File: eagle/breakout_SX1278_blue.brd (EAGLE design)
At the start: 28.6 x 28.6 mm, 18 parts, among them X1 734120110

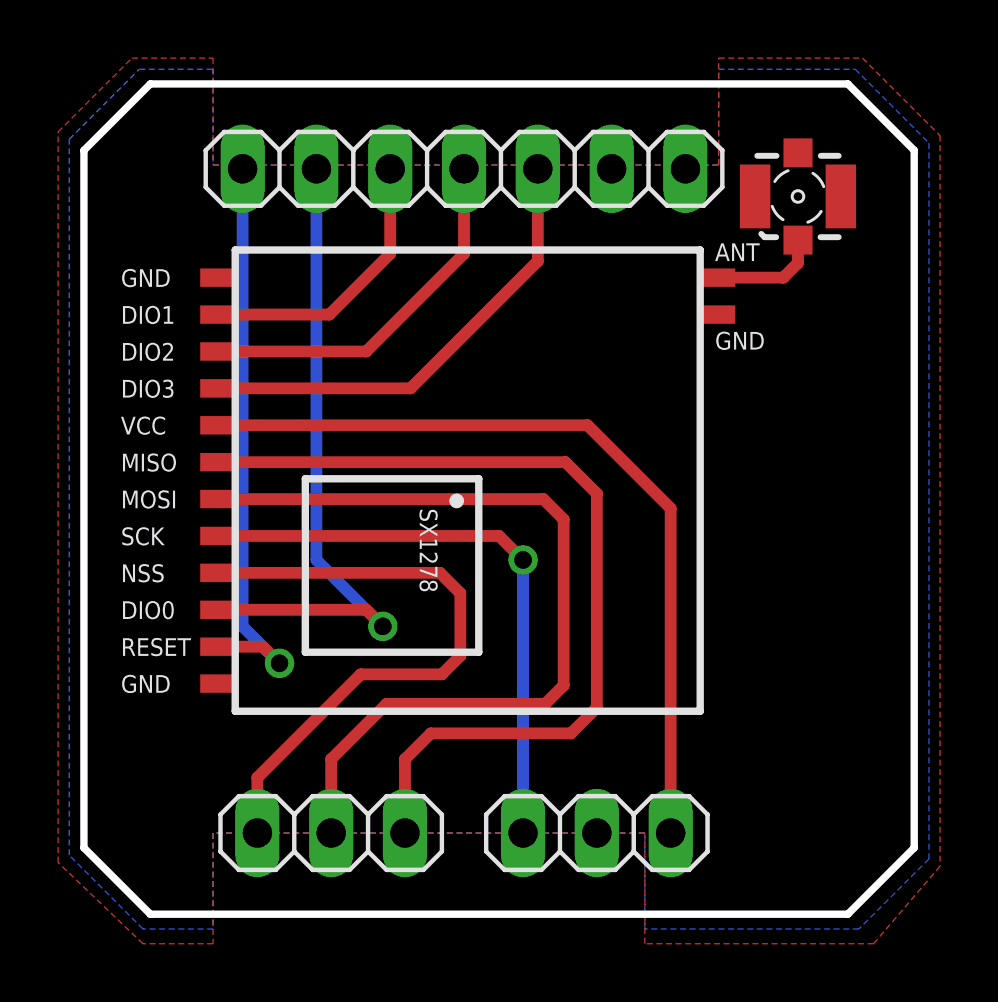
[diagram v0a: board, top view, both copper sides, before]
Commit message: Major layout update, read details
The layouts of shield and all breakout boards were changed to match the new multiprotocol standard.
IMPORTANT: The new shield is NOT compatible with the old breakout boards!
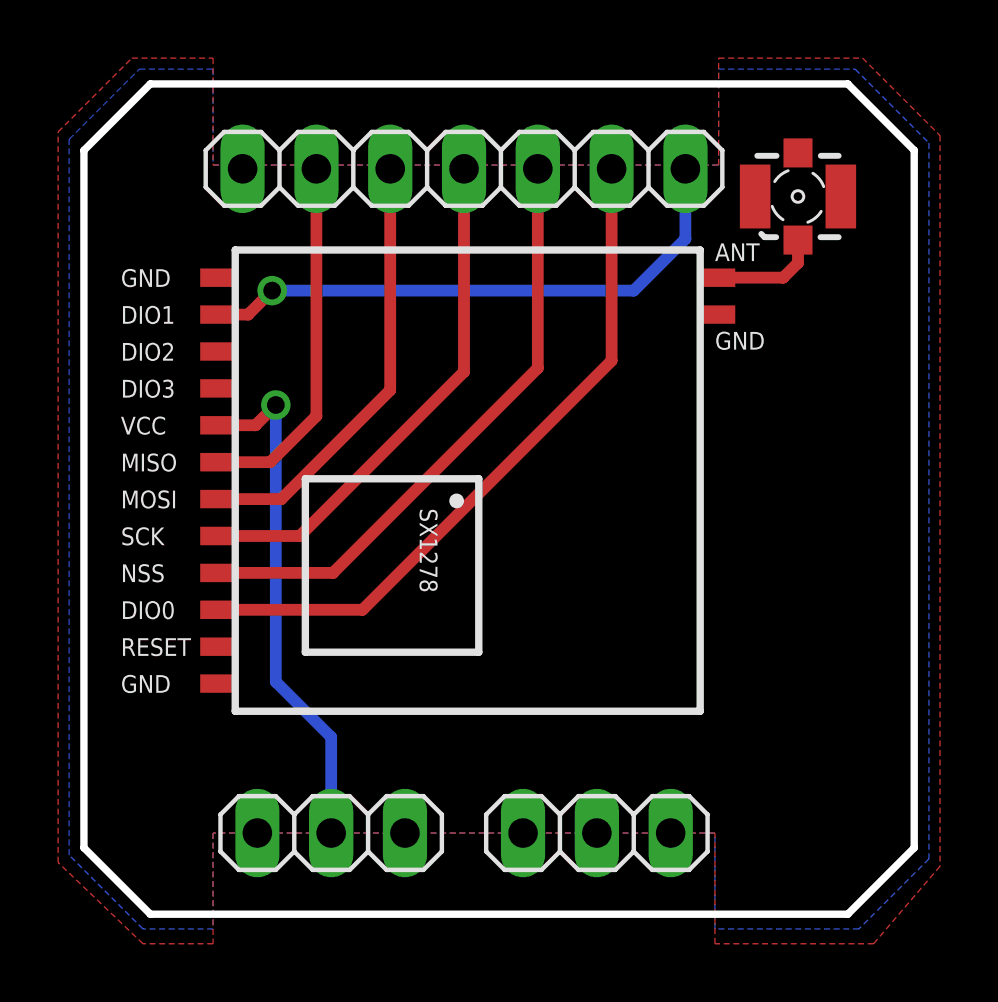
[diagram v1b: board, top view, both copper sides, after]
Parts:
- renumbered JP1 to CON_2, JP2A to CON_1, JP2B to CON_0
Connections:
- removed net 3.3V: CON_1.1, VCC.1
- removed net DIO2: CON_2.4, DIO2.1
- removed net DIO3: CON_2.5, DIO3.1
- removed net RESET: CON_2.1, RESET.1
- new net VCC: CON_0.2, VCC.1
- net DIO0: now also CON_2.6; no longer CON_2.2
- net DIO1: now also CON_2.7; no longer CON_2.3
- net GND: now also CON_0.3; no longer CON_1.2
- net MISO: now also CON_2.2; no longer CON_0.1
- net MOSI: now also CON_2.3; no longer CON_0.2
- net NSS: now also CON_2.5; no longer CON_0.3
- net SCK: now also CON_2.4; no longer CON_1.3
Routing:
- net 3.3V: track 27.9 -> 0.00 mm
- net RESET: track 19.9 -> 0.00 mm, vias 1 -> 0
- net MISO: track 30.7 -> 12.5 mm
- net VCC: track 0.00 -> 17.8 mm, vias 0 -> 1
- net DIO3: track 16.0 -> 0.00 mm
- net MOSI: track 29.5 -> 15.1 mm
- net DIO2: track 12.8 -> 0.00 mm
- net DIO1: track 9.69 -> 19.6 mm, vias 0 -> 1
- net SCK: track 20.2 -> 17.8 mm, vias 1 -> 0
- net DIO0: track 22.6 -> 23.7 mm, vias 1 -> 0
- net NSS: track 21.4 -> 20.8 mm

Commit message: Fixed power connector orientation
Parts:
- flipped CON_0 to the bottom
- flipped CON_1 to the bottom
- renumbered VCC to 3.3V
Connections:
- net VCC renamed 3.3V
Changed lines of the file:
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@@
 <wire x1="26.289" y1="28.575" x2="2.286" y2="28.575" width="0.254" layer="20"/>
 <wire x1="2.286" y1="28.575" x2="0" y2="26.289" width="0.254" layer="20"/>
-<wire x1="5.207" y1="22.86" x2="21.209" y2="22.86" width="0.254" layer="21"/>
-<wire x1="21.209" y1="22.86" x2="21.209" y2="6.985" width="0.254" layer="21"/>
-<wire x1="21.209" y1="6.985" x2="5.207" y2="6.985" width="0.254" layer="21"/>
-<wire x1="5.207" y1="6.985" x2="5.207" y2="22.86" width="0.254" layer="21"/>
+<wire x1="5.207" y1="22.86" x2="21.209" y2="22.86" width="0.254" layer="51"/>
+<wire x1="21.209" y1="22.86" x2="21.209" y2="6.985" width="0.254" layer="51"/>
+<wire x1="21.209" y1="6.985" x2="5.207" y2="6.985" width="0.254" layer="51"/>
+<wire x1="5.207" y1="6.985" x2="5.207" y2="22.86" width="0.254" layer="51"/>
 <text x="21.717" y="19.431" size="0.6096" layer="25" rot="SR0">GND</text>
 <wire x1="7.62" y1="9.017" x2="13.589" y2="9.017" width="0.254" layer="21"/>
@@
 <circle x="12.827" y="14.224" radius="0.127" width="0.254" layer="21"/>
 <text x="1.27" y="7.62" size="0.6096" layer="25">GND</text>
+<wire x1="5.207" y1="22.606" x2="5.207" y2="22.86" width="0.254" layer="21"/>
+<wire x1="5.207" y1="22.86" x2="21.209" y2="22.86" width="0.254" layer="21"/>
+<wire x1="21.209" y1="22.86" x2="21.209" y2="22.606" width="0.254" layer="21"/>
+<wire x1="21.209" y1="19.939" x2="21.209" y2="6.985" width="0.254" layer="21"/>
+<wire x1="21.209" y1="6.985" x2="5.207" y2="6.985" width="0.254" layer="21"/>
+<wire x1="5.207" y1="6.985" x2="5.207" y2="7.239" width="0.254" layer="21"/>
 </plain>
 <attributes>
@@
 <attribute name="NAME" x="21.717" y="22.479" size="0.6096" layer="25"/>
 </element>
-<element name="VCC" library="wirepad" package="SMD0,65-1,27" value="" x="4.6355" y="16.8275" smashed="yes" rot="R270">
+<element name="3.3V" library="wirepad" package="SMD0,65-1,27" value="" x="4.6355" y="16.8275" smashed="yes" rot="R270">
 <attribute name="NAME" x="1.27" y="16.51" size="0.6096" layer="25"/>
 </element>
@@
 </element>
 <element name="X1" library="con-coax" package="734120110" value="734120110" x="24.5745" y="24.7015" smashed="yes"/>
-<element name="CON_0" library="pinhead" package="1X03" value="" x="8.509" y="2.794" smashed="yes" rot="R180">
-<attribute name="VALUE" x="12.319" y="5.969" size="1.27" layer="27" rot="R180"/>
-</element>
-<element name="CON_1" library="pinhead" package="1X03" value="" x="17.653" y="2.794" smashed="yes" rot="R180">
-<attribute name="VALUE" x="21.463" y="5.969" size="1.27" layer="27" rot="R180"/>
+<element name="CON_0" library="pinhead" package="1X03" value="" x="8.509" y="2.794" smashed="yes" rot="MR180">
+<attribute name="VALUE" x="4.699" y="5.969" size="1.27" layer="28" rot="MR180"/>
+</element>
+<element name="CON_1" library="pinhead" package="1X03" value="" x="17.653" y="2.794" smashed="yes" rot="MR180">
+<attribute name="VALUE" x="13.843" y="5.969" size="1.27" layer="28" rot="MR180"/>
 </element>
 <element name="GND2" library="wirepad" package="SMD0,65-1,27" value="" x="4.6355" y="7.9375" smashed="yes" rot="R270"/>
@@
 <wire x1="20.701" y1="23.241" x2="20.701" y2="25.654" width="0.4064" layer="16"/>
 </signal>
-<signal name="VCC">
-<contactref element="VCC" pad="1"/>
+<signal name="3.3V">
+<contactref element="3.3V" pad="1"/>
 <contactref element="CON_0" pad="2"/>
 <wire x1="4.6355" y1="16.8275" x2="5.9055" y2="16.8275" width="0.4064" layer="1"/>
